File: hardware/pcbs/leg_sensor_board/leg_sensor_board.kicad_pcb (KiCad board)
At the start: 2 copper layers, 25 x 20 mm, 9 parts, among them J1 Conn_01x03, J2 Conn_01x02, U1 ATtiny202-SS, U2 FSA3157P6X

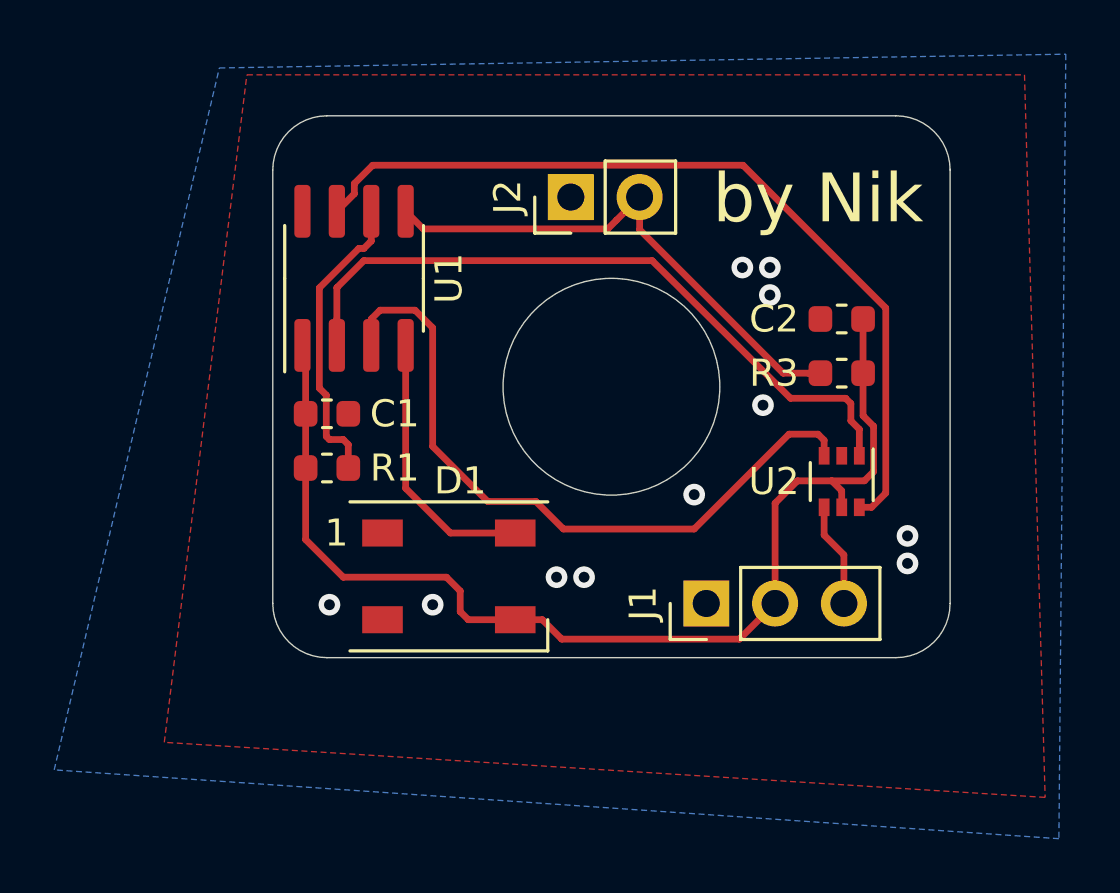
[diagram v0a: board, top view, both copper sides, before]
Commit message: fixed urdf and added pin names to pcb
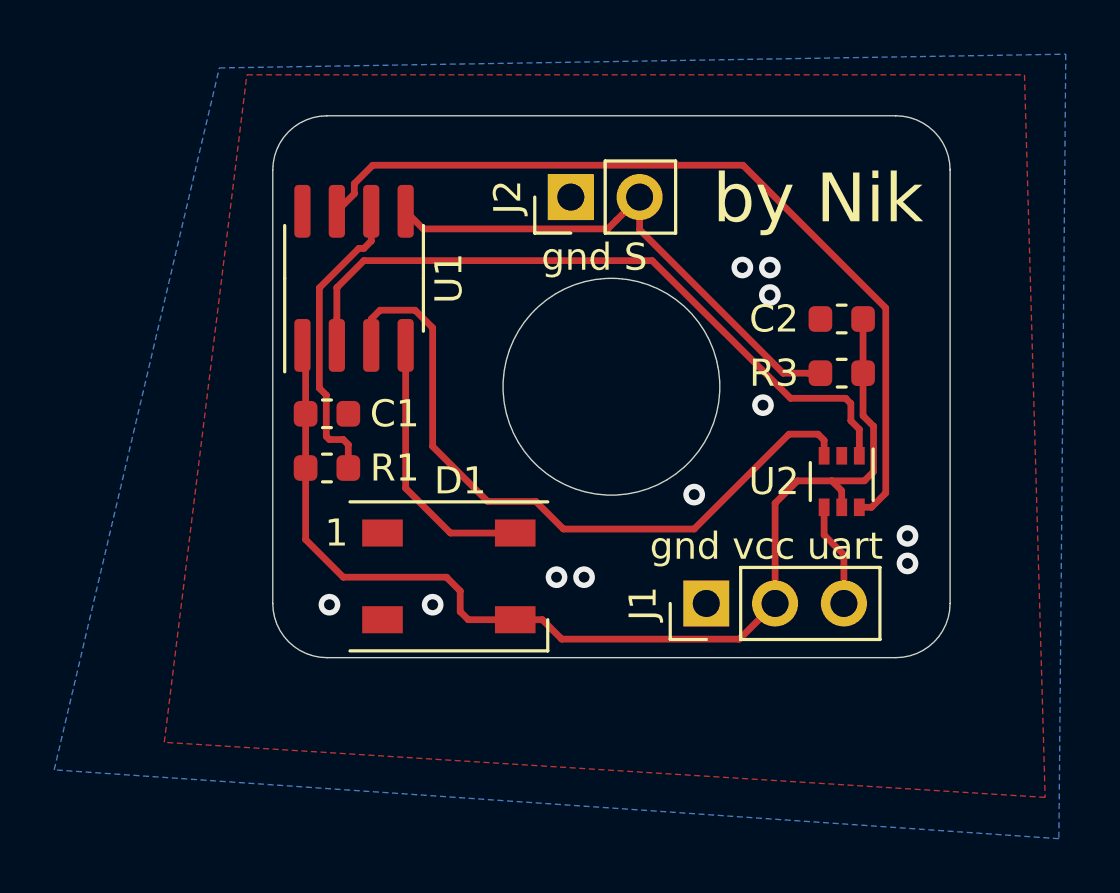
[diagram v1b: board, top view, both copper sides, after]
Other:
- board text added: "gnd S"
- board text added: "gnd vcc uart"
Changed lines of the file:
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@@
   (general
     (thickness 1.6)
-    (drawings 20)
+    (drawings 22)
     (tracks 92)
     (zones 0)
@@
       (net 2 UART))
   )
+  (gr_text "gnd vcc uart" (at 117.221 111.887) (layer F.SilkS)
+    (effects (font (size 1 1) (thickness 0.15)))
+  )
+  (gr_text "gnd S" (at 110.871 101.219) (layer F.SilkS)
+    (effects (font (size 1 1) (thickness 0.15)))
+  )
   (gr_text "by Nik" (at 119.126 99.06) (layer F.SilkS)
